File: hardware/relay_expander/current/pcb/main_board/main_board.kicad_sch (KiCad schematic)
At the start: 12 parts, among them J1 Conn_01x07_Socket, J2 Screw_Terminal_01x02, J3 Conn_01x07_Socket, U1 MCP23017x-x-SO

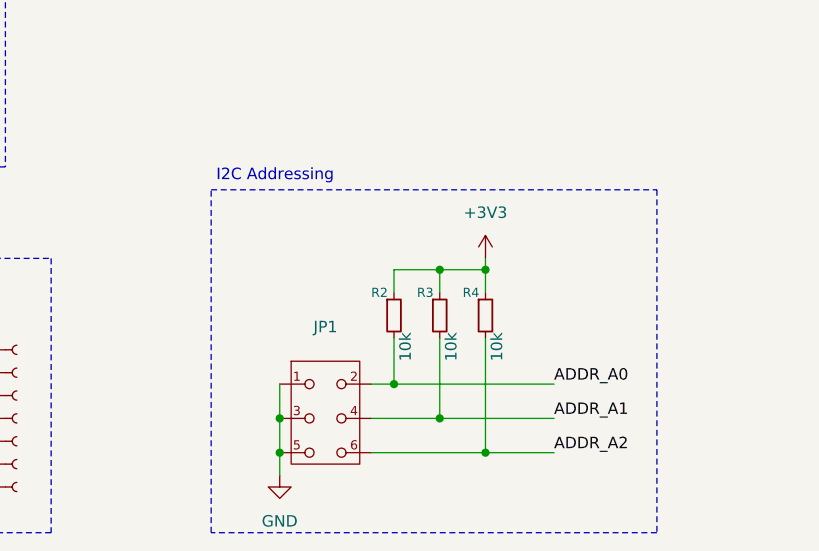
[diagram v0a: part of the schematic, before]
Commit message: [CHANGE] i2c adressing
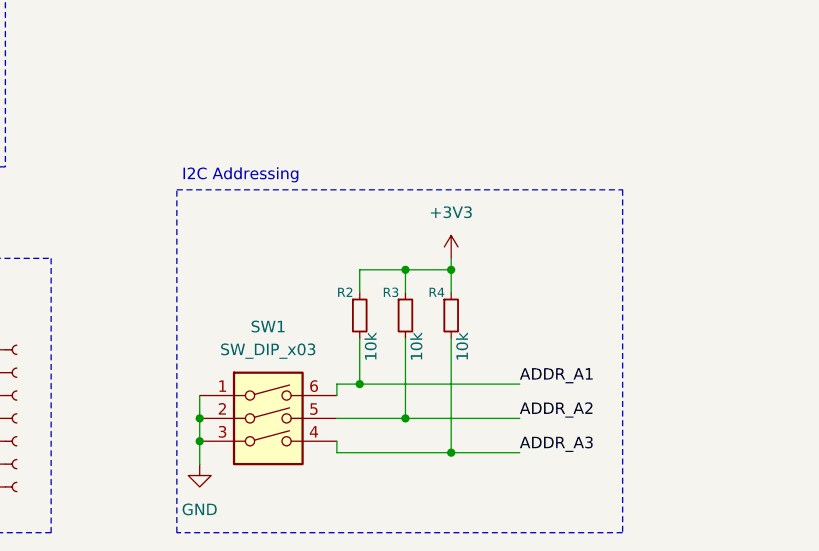
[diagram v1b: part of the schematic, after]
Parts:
- removed JP1: (no value), Connector_PinHeader_2.54mm:PinHeader_2x03_P2.54mm_Vertical, symbol templates_lib:Jumper_Wire_x3
- added SW1: SW_DIP_x03, Button_Switch_THT:SW_DIP_SPSTx03_Slide_6.7x9.18mm_W7.62mm_P2.54mm_LowProfile, symbol Switch:SW_DIP_x03
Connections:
- net ADDR_A0: no longer R2.2
- net ADDR_A1: now also R2.2, SW1.6; no longer R3.2
- net ADDR_A2: now also R3.2, SW1.5; no longer R4.2
- net GND: now also SW1.1, SW1.2, SW1.3
- new net ADDR_A3: R4.2, SW1.4

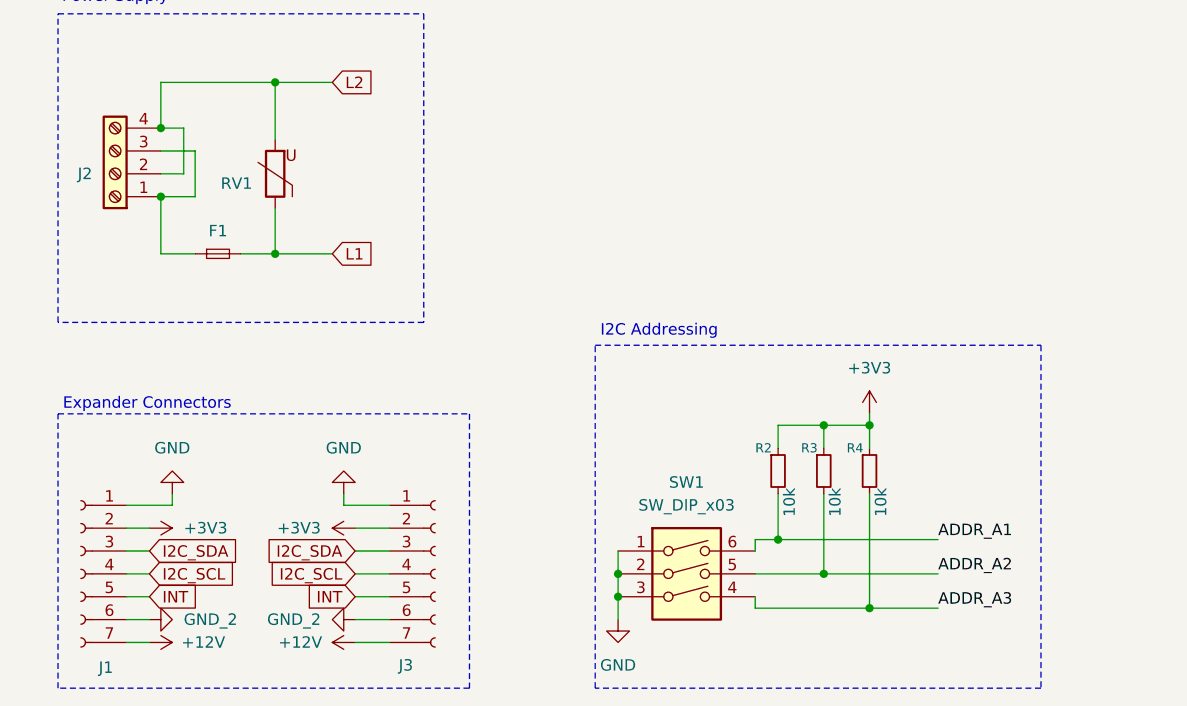
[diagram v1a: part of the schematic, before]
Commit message: [ADD] lauout for relay expander pcb
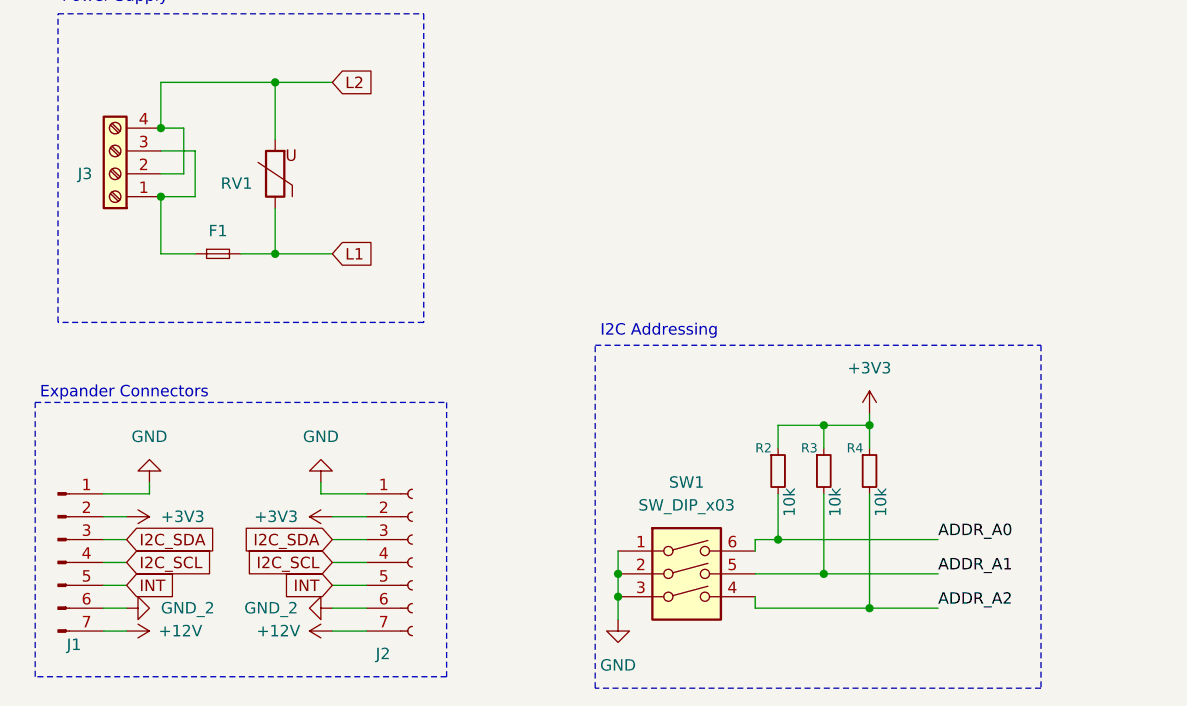
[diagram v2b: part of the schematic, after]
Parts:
- removed J1: Conn_01x07_Socket, templates_lib_footprints:PinSocket_1x07_P2.54mm_Horizontal, symbol Connector:Conn_01x07_Socket
- removed J3: Conn_01x07_Socket, templates_lib_footprints:PinSocket_1x07_P2.54mm_Horizontal_Right, symbol Connector:Conn_01x07_Socket
- added J1: Conn_01x07_Socket, homeautomation_core:PinHeader_1x07_P2.54mm_Horizontal_left, symbol Connector:Conn_01x07_Pin
- added J2: Conn_01x07_Socket, homeautomation_core:PinSocket_1x07_P2.54mm_Horizontal_Right, symbol Connector:Conn_01x07_Socket
- renumbered J2 to J3
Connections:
- net ADDR_A3 is gone; now on net ADDR_A2: R4.2, SW1.4
- net +12V: now also J1.7 (Pin_7), J2.7 (Pin_7)
- net +3V3: now also J1.2 (Pin_2), J2.2 (Pin_2)
- net ADDR_A0: now also R2.2, SW1.6
- net ADDR_A1: now also R3.2, SW1.5; no longer R2.2, SW1.6
- net ADDR_A2: no longer R3.2, SW1.5
- net GND: now also J1.1 (Pin_1), J2.1 (Pin_1)
- net GND_2: now also J1.6 (Pin_6), J2.6 (Pin_6)
- net I2C_SCL: now also J1.4 (Pin_4), J2.4 (Pin_4)
- net I2C_SDA: now also J1.3 (Pin_3), J2.3 (Pin_3)
- net INT: now also J1.5 (Pin_5), J2.5 (Pin_5)
